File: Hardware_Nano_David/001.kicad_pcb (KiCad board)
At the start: 2 copper layers, 62.2 x 81.8 mm, 22 parts, among them J1 New_Arduino_NANO, U1 NANO_ALL_PCB, U2 Firma, U3 OSH

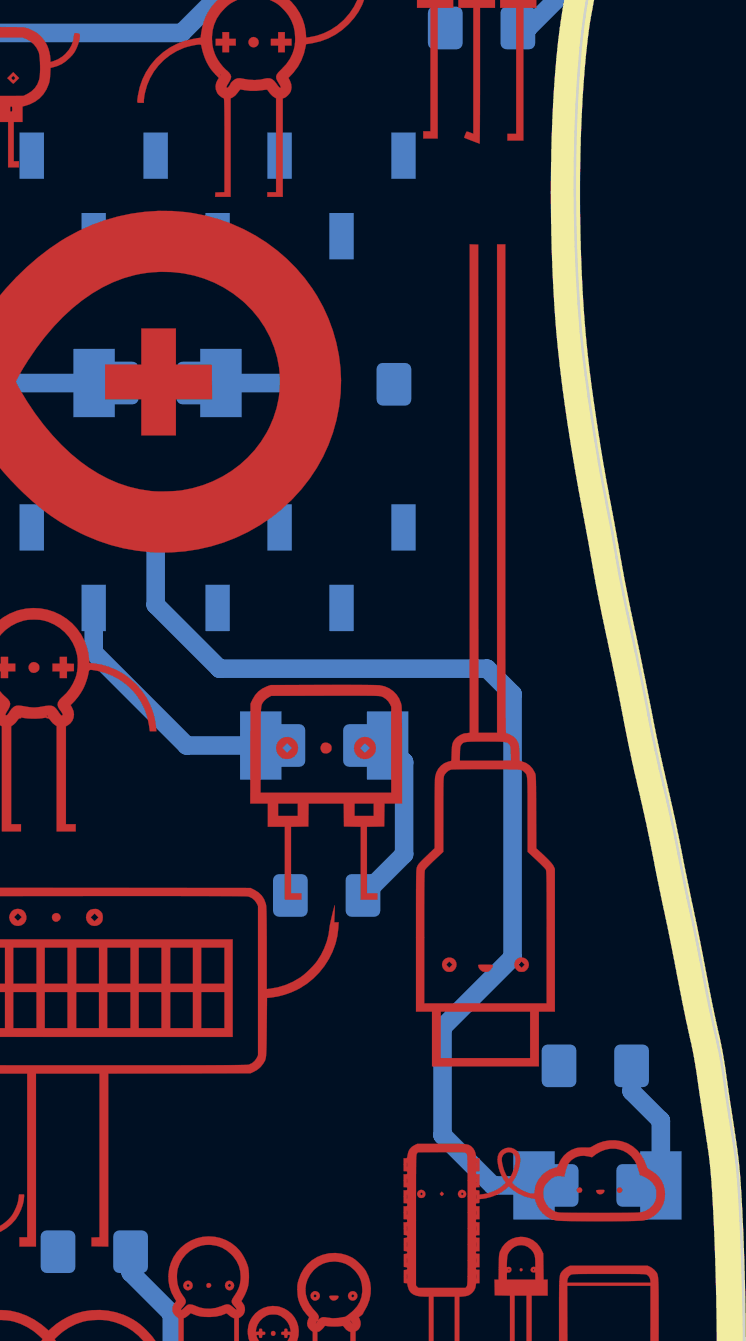
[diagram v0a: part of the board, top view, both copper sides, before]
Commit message: Add LIPO battery
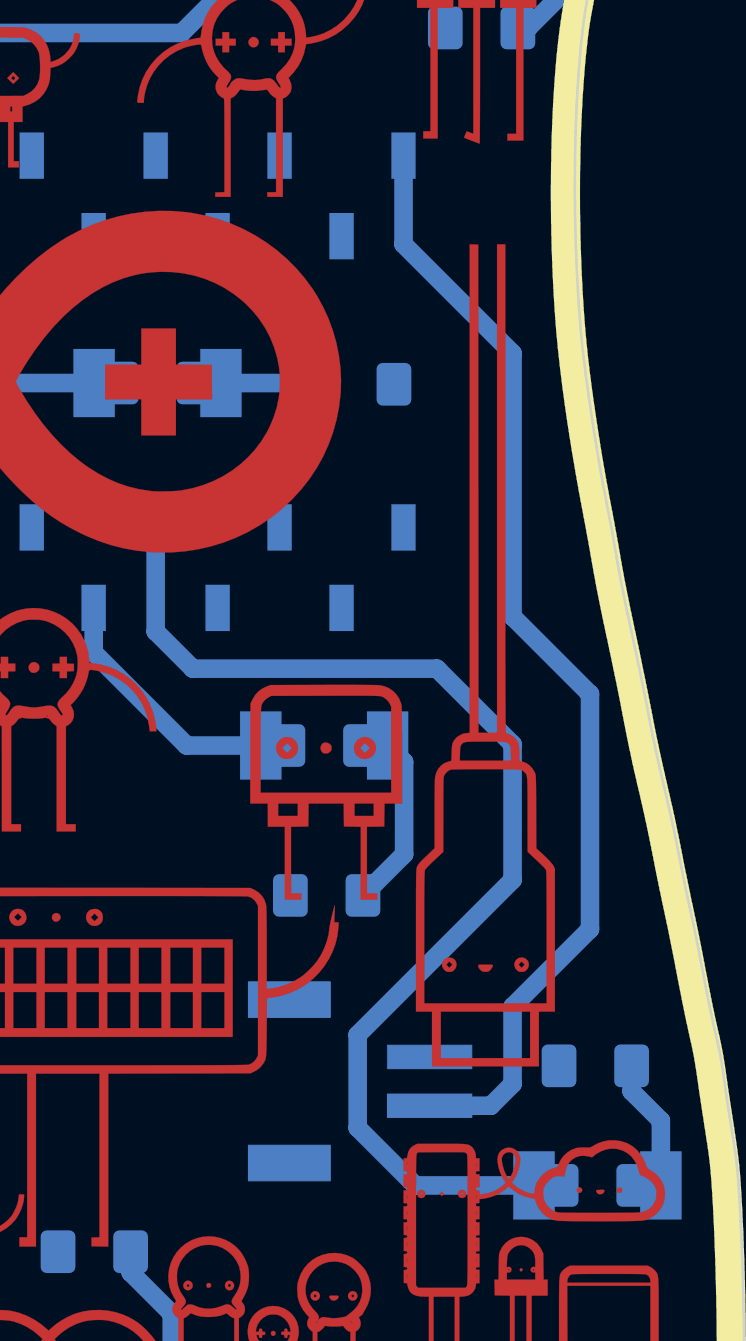
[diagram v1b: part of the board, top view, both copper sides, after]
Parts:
- added J2: Conn_01x02, NANO_Badge_01:JST-S2B-PH-SM4-TB, B.Cu at (154.9, 102.2)
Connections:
- J1 pad 15: (no net) -> VIN
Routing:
- net VIN: track 0.00 -> 46.3 mm
- net /~D2: track 44.3 -> 48.5 mm
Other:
- board text added: "+"
- board text added: "-"
